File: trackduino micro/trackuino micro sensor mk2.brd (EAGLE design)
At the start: 43.3 x 19.1 mm, 42 parts, among them IC2 74AHC1G125DBV, SW1 SPST_TACT-KMR2, U1 ATMEGA168MLF, Y1 16MHZ

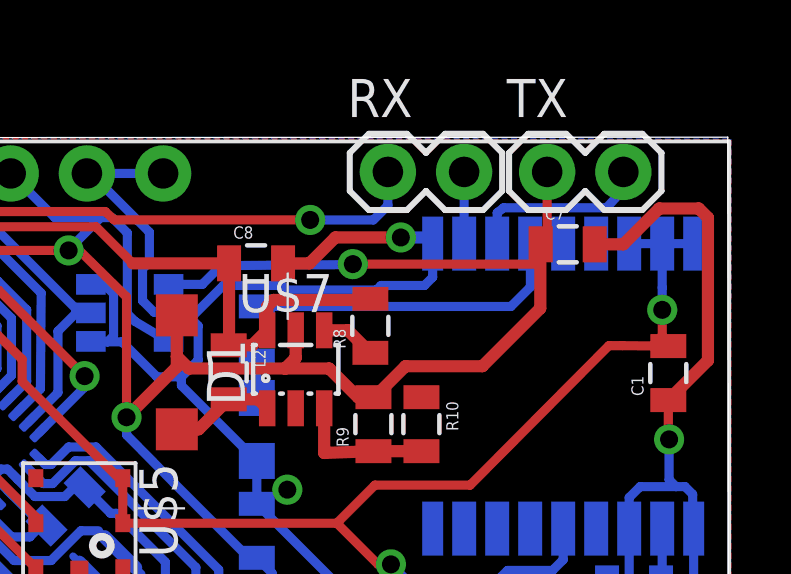
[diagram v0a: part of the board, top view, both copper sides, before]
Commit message: sensor mk2 fixes
fixed a short on the boost output and serial RX
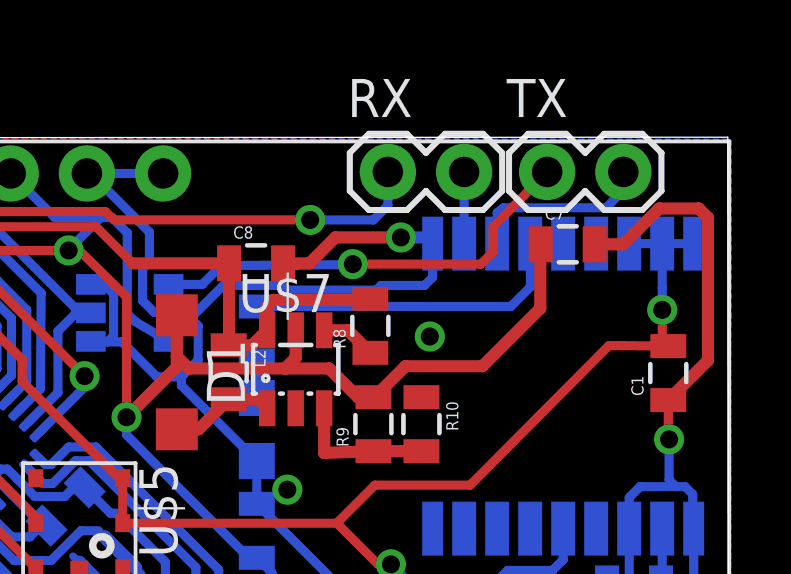
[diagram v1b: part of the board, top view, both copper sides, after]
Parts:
- C7: value (none) -> 22uf
- C8: value (none) -> 10uf
- L2: value (none) -> 2.2uh
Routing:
- net TX1: track 15.7 -> 14.7 mm
- net GND: vias 4 -> 5
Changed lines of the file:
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@@
 <element name="U$7" library="adafruit" package="SOT23-6" value="LT3426" x="80.2132" y="68.834"/>
 <element name="D1" library="diode" package="SOD123" value="" x="76.2508" y="68.7324" rot="R270"/>
-<element name="L2" library="SparkFun-Passives" package="0805" value="" x="77.978" y="68.7324" rot="R270"/>
+<element name="L2" library="SparkFun-Passives" package="0805" value="2.2uh" x="77.978" y="68.7324" rot="R270"/>
 <element name="R8" library="SparkFun-Resistors" package="0805" value="" x="82.7024" y="70.2818" rot="R90"/>
 <element name="R9" library="SparkFun-Resistors" package="0805" value="" x="82.804" y="67.0052" rot="R90"/>
 <element name="R10" library="SparkFun-Resistors" package="0805" value="" x="84.4042" y="67.0052" rot="R270"/>
-<element name="C7" library="SparkFun-Capacitors" package="0805" value="" x="89.281" y="72.9996"/>
-<element name="C8" library="SparkFun-Capacitors" package="0805" value="" x="78.8924" y="72.3646"/>
+<element name="C7" library="SparkFun-Capacitors" package="0805" value="22uf" x="89.281" y="72.9996"/>
+<element name="C8" library="SparkFun-Capacitors" package="0805" value="10uf" x="78.8924" y="72.3646"/>
 </elements>
 <signals>
@@
 <wire x1="93.9546" y1="73.8886" x2="93.9546" y2="69.1278" width="0.4064" layer="1"/>
 <wire x1="93.9546" y1="69.1278" x2="92.6338" y2="67.807" width="0.4064" layer="1"/>
+<via x="84.6836" y="69.9262" extent="1-16" drill="0.6" shape="square"/>
 <wire x1="56.5658" y1="58.6486" x2="56.5912" y2="58.674" width="0" layer="19" extent="1-1"/>
 <wire x1="52.1884" y1="67.183" x2="53.3908" y2="63.754" width="0" layer="19" extent="1-16"/>
@@
 <wire x1="82.103" y1="72.324" x2="82.1182" y2="72.3392" width="0.3048" layer="16"/>
 <via x="82.1182" y="72.3392" extent="1-16" drill="0.6" shape="square"/>
-<wire x1="82.1182" y1="72.3392" x2="88.2142" y2="72.3392" width="0.3048" layer="1"/>
-<wire x1="88.2142" y1="72.3392" x2="88.5952" y2="72.7202" width="0.3048" layer="1"/>
-<wire x1="88.5952" y1="72.7202" x2="88.5952" y2="75.4126" width="0.3048" layer="1"/>
+<wire x1="82.1182" y1="72.3392" x2="86.3854" y2="72.3392" width="0.3048" layer="1"/>
+<wire x1="86.3854" y1="72.3392" x2="86.7918" y2="72.7456" width="0.3048" layer="1"/>
+<wire x1="86.7918" y1="72.7456" x2="86.7918" y2="73.5838" width="0.3048" layer="1"/>
+<wire x1="86.7918" y1="73.5838" x2="87.1728" y2="73.9648" width="0.3048" layer="1"/>
+<wire x1="87.1728" y1="73.9648" x2="88.5952" y2="75.4126" width="0.3048" layer="1"/>
 </signal>
 <signal name="VDDD">

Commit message: fixed ground plane  bit
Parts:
- moved R8 1.24 mm to (83.9, 70.3)
- moved R10 1.12 mm to (85.5, 67.0)
- moved R9 1.07 mm to (83.9, 67.0)
- moved U$7 1.04 mm to (81.3, 68.8)
- moved L2 0.51 mm to (78.5, 68.7)
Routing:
- net N$13: track 4.73 -> 1.65 mm
- net N$9: track 3.55 -> 4.59 mm
- net 15V: track 33.3 -> 34.3 mm
- net GND: vias 5 -> 6
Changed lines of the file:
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@@
 <element name="R3" library="SparkFun-Resistors" package="0805" value="" x="61.6458" y="69.85"/>
 <element name="R7" library="SparkFun-Resistors" package="0805" value="" x="65.0748" y="69.8246"/>
-<element name="U$7" library="adafruit" package="SOT23-6" value="LT3426" x="80.2132" y="68.834"/>
+<element name="U$7" library="adafruit" package="SOT23-6" value="LT3426" x="81.2546" y="68.834"/>
 <element name="D1" library="diode" package="SOD123" value="" x="76.2508" y="68.7324" rot="R270"/>
-<element name="L2" library="SparkFun-Passives" package="0805" value="2.2uh" x="77.978" y="68.7324" rot="R270"/>
-<element name="R8" library="SparkFun-Resistors" package="0805" value="" x="82.7024" y="70.2818" rot="R90"/>
-<element name="R9" library="SparkFun-Resistors" package="0805" value="" x="82.804" y="67.0052" rot="R90"/>
-<element name="R10" library="SparkFun-Resistors" package="0805" value="" x="84.4042" y="67.0052" rot="R270"/>
+<element name="L2" library="SparkFun-Passives" package="0805" value="2.2uh" x="78.486" y="68.7324" rot="R270"/>
+<element name="R8" library="SparkFun-Resistors" package="0805" value="" x="83.947" y="70.3072" rot="R90"/>
+<element name="R9" library="SparkFun-Resistors" package="0805" value="" x="83.8708" y="67.0052" rot="R90"/>
+<element name="R10" library="SparkFun-Resistors" package="0805" value="" x="85.5218" y="66.9798" rot="R270"/>
 <element name="C7" library="SparkFun-Capacitors" package="0805" value="22uf" x="89.281" y="72.9996"/>
 <element name="C8" library="SparkFun-Capacitors" package="0805" value="10uf" x="78.8924" y="72.3646"/>
@@
 <wire x1="93.9546" y1="73.8886" x2="93.9546" y2="69.1278" width="0.4064" layer="1"/>
 <wire x1="93.9546" y1="69.1278" x2="92.6338" y2="67.807" width="0.4064" layer="1"/>
-<via x="84.6836" y="69.9262" extent="1-16" drill="0.6" shape="square"/>
+<via x="85.725" y="70.0024" extent="1-16" drill="0.6" shape="square"/>
+<via x="60.7822" y="64.9986" extent="1-16" drill="0.6" shape="square"/>
 <wire x1="56.5658" y1="58.6486" x2="56.5912" y2="58.674" width="0" layer="19" extent="1-1"/>
-<wire x1="52.1884" y1="67.183" x2="53.3908" y2="63.754" width="0" layer="19" extent="1-16"/>
-<wire x1="72.9996" y1="62.2032" x2="72.79173125" y2="62.602590625" width="0" layer="19" extent="1-16"/>
+<wire x1="60.7822" y1="64.9986" x2="58.293" y2="63.754" width="0" layer="19" extent="1-1"/>
 </signal>
 <signal name="VCC">
@@
 <wire x1="74.5744" y1="66.6496" x2="74.5744" y2="67.2338" width="0.3048" layer="16"/>
 <via x="74.5744" y="67.2338" extent="1-16" drill="0.6" shape="square"/>
-<wire x1="74.5744" y1="67.2338" x2="74.5744" y2="71.247" width="0.3048" layer="1"/>
+<wire x1="74.5744" y1="67.2338" x2="74.5744" y2="71.0946" width="0.3048" layer="1"/>
+<wire x1="74.5744" y1="71.0946" x2="74.5744" y2="71.247" width="0.3048" layer="1"/>
 <wire x1="74.5744" y1="71.247" x2="72.9996" y2="72.7964" width="0.3048" layer="1"/>
 <wire x1="72.9996" y1="72.7964" x2="72.644" y2="72.7964" width="0.3048" layer="1"/>
@@
 <contactref element="R9" pad="2"/>
 <contactref element="C7" pad="1"/>
-<wire x1="76.2508" y1="70.6324" x2="76.2508" y2="69.2658" width="0.4064" layer="1"/>
-<wire x1="76.2508" y1="69.2658" x2="76.2508" y2="68.9102" width="0.4064" layer="1"/>
-<wire x1="76.2508" y1="68.9102" x2="74.5744" y2="67.2338" width="0.4064" layer="1"/>
-<wire x1="80.2132" y1="70.134" x2="80.2132" y2="69.215" width="0.4064" layer="1"/>
-<wire x1="80.2132" y1="69.215" x2="79.8576" y2="68.8594" width="0.4064" layer="1"/>
-<wire x1="79.8576" y1="68.8594" x2="76.6572" y2="68.8594" width="0.4064" layer="1"/>
-<wire x1="76.6572" y1="68.8594" x2="76.2508" y2="69.2658" width="0.4064" layer="1"/>
-<wire x1="79.8576" y1="68.8594" x2="81.3308" y2="68.8594" width="0.4064" layer="1"/>
-<wire x1="81.3308" y1="68.8594" x2="82.296" y2="67.8942" width="0.4064" layer="1"/>
-<wire x1="82.296" y1="67.8942" x2="82.793" y2="67.8942" width="0.4064" layer="1"/>
-<wire x1="82.793" y1="67.8942" x2="82.804" y2="67.9052" width="0.4064" layer="1"/>
-<wire x1="82.804" y1="67.9052" x2="82.8404" y2="67.9052" width="0.4064" layer="1"/>
-<wire x1="82.8404" y1="67.9052" x2="83.8708" y2="68.9356" width="0.4064" layer="1"/>
-<wire x1="83.8708" y1="68.9356" x2="86.4362" y2="68.9356" width="0.4064" layer="1"/>
-<wire x1="86.4362" y1="68.9356" x2="88.3666" y2="70.866" width="0.4064" layer="1"/>
-<wire x1="88.3666" y1="70.866" x2="88.3666" y2="72.9852" width="0.4064" layer="1"/>
 <wire x1="88.3666" y1="72.9852" x2="88.381" y2="72.9996" width="0.4064" layer="1"/>
+<wire x1="76.2508" y1="70.6324" x2="75.0366" y2="70.6324" width="0.4064" layer="1"/>
+<wire x1="75.0366" y1="70.6324" x2="74.5744" y2="71.0946" width="0.4064" layer="1"/>
+<wire x1="76.2508" y1="70.6324" x2="76.2508" y2="69.4436" width="0.4064" layer="1"/>
+<wire x1="76.2508" y1="69.4436" x2="76.9112" y2="68.7832" width="0.4064" layer="1"/>
+<wire x1="76.9112" y1="68.7832" x2="80.8736" y2="68.7832" width="0.4064" layer="1"/>
+<wire x1="80.8736" y1="68.7832" x2="81.2292" y2="69.1388" width="0.4064" layer="1"/>
+<wire x1="81.2292" y1="69.1388" x2="81.2292" y2="70.1086" width="0.4064" layer="1"/>
+<wire x1="81.2292" y1="70.1086" x2="81.2546" y2="70.134" width="0.4064" layer="1"/>
+<wire x1="83.8708" y1="67.9052" x2="83.555" y2="67.9052" width="0.4064" layer="1"/>
+<wire x1="83.555" y1="67.9052" x2="82.7278" y2="68.7324" width="0.4064" layer="1"/>
+<wire x1="82.7278" y1="68.7324" x2="81.6356" y2="68.7324" width="0.4064" layer="1"/>
+<wire x1="81.6356" y1="68.7324" x2="81.2292" y2="69.1388" width="0.4064" layer="1"/>
+<wire x1="83.8708" y1="67.9052" x2="84.0088" y2="67.9052" width="0.4064" layer="1"/>
+<wire x1="84.0088" y1="67.9052" x2="84.9884" y2="68.8848" width="0.4064" layer="1"/>
+<wire x1="84.9884" y1="68.8848" x2="87.376" y2="68.8848" width="0.4064" layer="1"/>
+<wire x1="87.376" y1="68.8848" x2="88.392" y2="69.9008" width="0.4064" layer="1"/>
+<wire x1="88.392" y1="69.9008" x2="88.392" y2="72.9886" width="0.4064" layer="1"/>
+<wire x1="88.392" y1="72.9886" x2="88.381" y2="72.9996" width="0.4064" layer="1"/>
 </signal>
 <signal name="D3">
@@
 <contactref element="R8" pad="2"/>
 <contactref element="C8" pad="1"/>
-<wire x1="77.978" y1="69.6324" x2="78.7616" y2="69.6324" width="0.4064" layer="1"/>
-<wire x1="78.7616" y1="69.6324" x2="79.2632" y2="70.134" width="0.4064" layer="1"/>
 <wire x1="77.9924" y1="72.3646" x2="77.9924" y2="69.6468" width="0.4064" layer="1"/>
-<wire x1="77.9924" y1="69.6468" x2="77.978" y2="69.6324" width="0.4064" layer="1"/>
+<wire x1="77.9924" y1="69.6468" x2="78.486" y2="69.6324" width="0.4064" layer="1"/>
 <wire x1="74.7776" y1="72.3646" x2="77.9924" y2="72.3646" width="0.4064" layer="1"/>
-<wire x1="79.2632" y1="70.134" x2="79.2632" y2="70.932" width="0.4064" layer="1"/>
-<wire x1="79.2632" y1="70.932" x2="79.4766" y2="71.1454" width="0.4064" layer="1"/>
-<wire x1="79.4766" y1="71.1454" x2="82.8184" y2="71.1454" width="0.4064" layer="1"/>
-<wire x1="82.8184" y1="71.1454" x2="82.7024" y2="71.1818" width="0.4064" layer="1"/>
+<wire x1="78.486" y1="69.6324" x2="79.803" y2="69.6324" width="0.4064" layer="1"/>
+<wire x1="79.803" y1="69.6324" x2="80.3046" y2="70.134" width="0.4064" layer="1"/>
+<wire x1="80.3046" y1="70.134" x2="80.3046" y2="70.9574" width="0.4064" layer="1"/>
+<wire x1="80.3046" y1="70.9574" x2="80.5434" y2="71.1962" width="0.4064" layer="1"/>
+<wire x1="80.5434" y1="71.1962" x2="83.936" y2="71.1962" width="0.4064" layer="1"/>
+<wire x1="83.936" y1="71.1962" x2="83.947" y2="71.2072" width="0.4064" layer="1"/>
 </signal>
 <signal name="N$7">
@@
 <contactref element="L2" pad="2"/>
 <contactref element="L2" pad="2"/>
-<wire x1="76.2508" y1="66.8324" x2="76.978" y2="66.8324" width="0.4064" layer="1"/>
-<wire x1="76.978" y1="66.8324" x2="77.978" y2="67.8324" width="0.4064" layer="1"/>
-<wire x1="77.978" y1="67.8324" x2="78.9648" y2="67.8324" width="0.4064" layer="1"/>
-<wire x1="78.9648" y1="67.8324" x2="79.2632" y2="67.534" width="0.4064" layer="1"/>
+<wire x1="76.2508" y1="66.8324" x2="77.486" y2="66.8324" width="0.4064" layer="1"/>
+<wire x1="77.486" y1="66.8324" x2="78.486" y2="67.8324" width="0.4064" layer="1"/>
+<wire x1="78.486" y1="67.8324" x2="80.0062" y2="67.8324" width="0.4064" layer="1"/>
+<wire x1="80.0062" y1="67.8324" x2="80.3046" y2="67.534" width="0.4064" layer="1"/>
 </signal>
 <signal name="N$12">
 <contactref element="U$7" pad="4"/>
 <contactref element="R8" pad="1"/>
-<wire x1="81.1632" y1="70.134" x2="81.9502" y2="70.134" width="0.4064" layer="1"/>
-<wire x1="81.9502" y1="70.134" x2="82.7024" y2="69.3818" width="0.4064" layer="1"/>
+<wire x1="82.2046" y1="70.134" x2="83.2202" y2="70.134" width="0.4064" layer="1"/>
+<wire x1="83.2202" y1="70.134" x2="83.947" y2="69.4072" width="0.4064" layer="1"/>
 </signal>
 <signal name="N$13">
@@
 <contactref element="R10" pad="2"/>
 <contactref element="U$7" pad="3"/>
-<wire x1="81.1632" y1="67.534" x2="81.1632" y2="66.0442" width="0.4064" layer="1"/>
-<wire x1="81.1632" y1="66.0442" x2="82.804" y2="66.1052" width="0.4064" layer="1"/>
-<wire x1="82.804" y1="66.1052" x2="84.4042" y2="66.1052" width="0.4064" layer="1"/>
+<wire x1="83.8708" y1="66.1052" x2="85.5218" y2="66.0798" width="0.4064" layer="1"/>
+<wire x1="82.2046" y1="67.534" x2="83.8708" y2="66.1052" width="0" layer="19" extent="1-1"/>
 </signal>
 </signals>

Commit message: missing trace
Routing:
- net N$13: track 1.65 -> 4.54 mm
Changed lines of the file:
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@@
 <contactref element="U$7" pad="3"/>
 <wire x1="83.8708" y1="66.1052" x2="85.5218" y2="66.0798" width="0.4064" layer="1"/>
-<wire x1="82.2046" y1="67.534" x2="83.8708" y2="66.1052" width="0" layer="19" extent="1-1"/>
+<wire x1="82.2046" y1="67.534" x2="82.2046" y2="66.4616" width="0.4064" layer="1"/>
+<wire x1="82.2046" y1="66.4616" x2="82.55" y2="66.1162" width="0.4064" layer="1"/>
+<wire x1="82.55" y1="66.1162" x2="83.8598" y2="66.1162" width="0.4064" layer="1"/>
+<wire x1="83.8598" y1="66.1162" x2="83.8708" y2="66.1052" width="0.4064" layer="1"/>
 </signal>
 </signals>

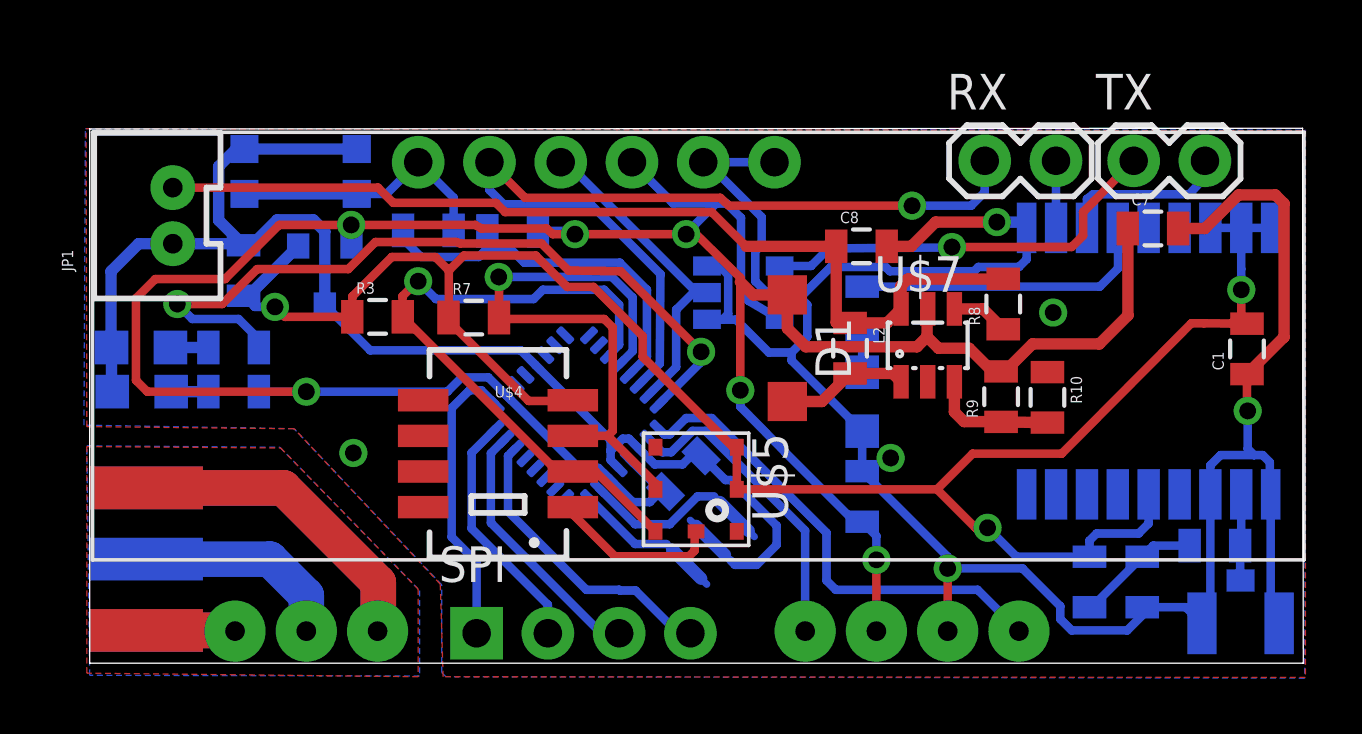
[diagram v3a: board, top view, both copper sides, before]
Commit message: DRC check
ran osh park DRC check and resolved errors.
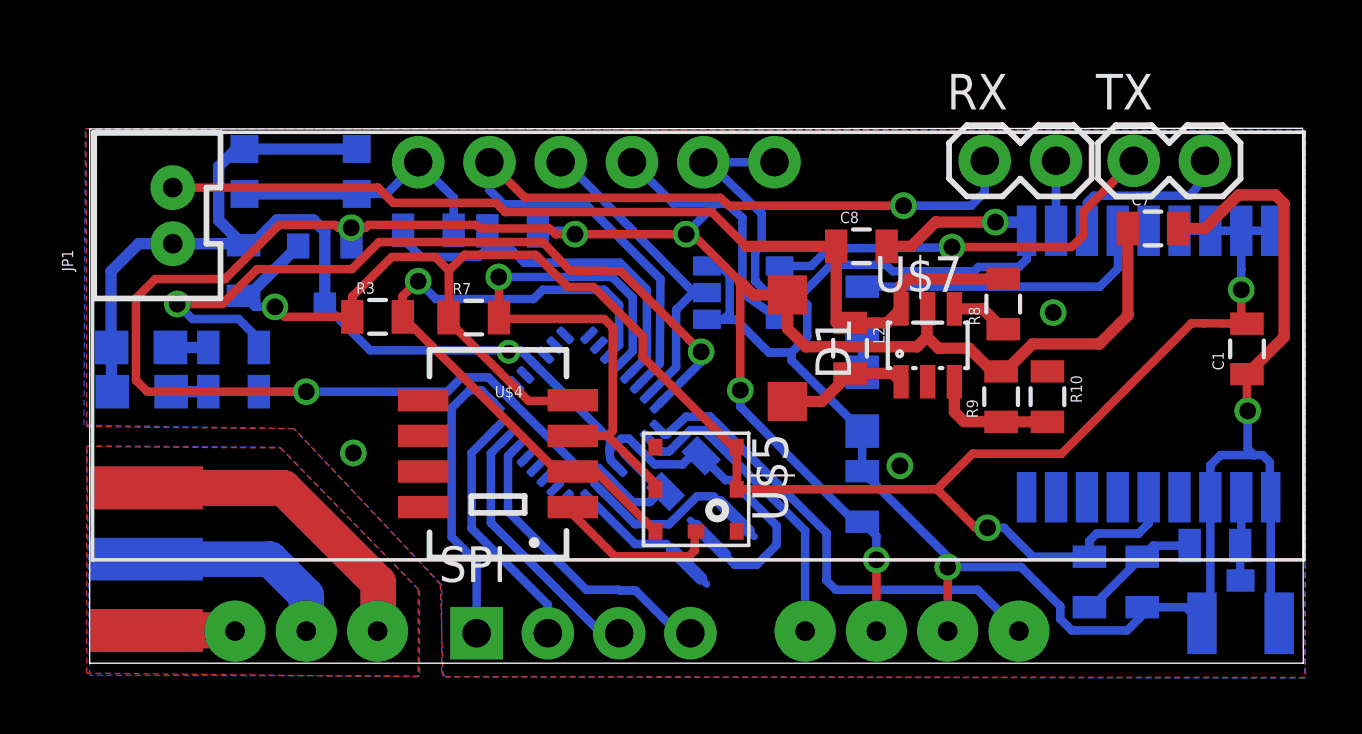
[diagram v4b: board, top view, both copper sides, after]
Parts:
- D1: value (none) -> MBR120VLSFT1
- R10: value (none) -> 30.9k
- R8: value (none) -> 1m
- R9: value (none) -> 95.3k
- moved U$1 0.10 mm to (89.2, 68.0)
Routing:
- net GND: track 167.4 -> 167.5 mm, vias 6 -> 7
